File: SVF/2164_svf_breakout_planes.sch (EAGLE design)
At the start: 87 parts, among them IC1 SSM2164P, IC2 TL072, IC3 TL072, IC4 TL072, IC5 TL072, IC6 TL072, U1 THONKICONNNEW, U2 THONKICONNNEW, U3 THONKICONNNEW, U4 THONKICONNNEW, U5 THONKICONNNEW, U6 THONKICONNNEW

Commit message: Add copyright notice
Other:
- note added: "Copyright (c) 2021 Janne Heikkarainen (janne808@radiofreerobotron.net) All rights reserved"
- note added: "Released under CERN Open Hardware Licence Version 2 - Strongly Reciprocal"
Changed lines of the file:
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@@
 <text x="40.64" y="132.08" size="1.778" layer="91">cv1</text>
 <text x="40.64" y="236.22" size="1.778" layer="91">cv2</text>
+<text x="170.18" y="15.24" size="1.778" layer="91">Copyright (c) 2021 Janne Heikkarainen (janne808@radiofreerobotron.net)
+All rights reserved
+</text>
+<text x="170.18" y="10.16" size="1.778" layer="91">Released under CERN Open Hardware Licence Version 2 - Strongly Reciprocal</text>
 </plain>
 <instances>
@@
 </drawing>
 <compatibility>
+<note version="6.3" minversion="6.2.2" severity="warning">
+Since Version 6.2.2 text objects can contain more than one line,
+which will not be processed correctly with this version.
+</note>
 <note version="8.2" severity="warning">
 Since Version 8.2, EAGLE supports online libraries. The ids

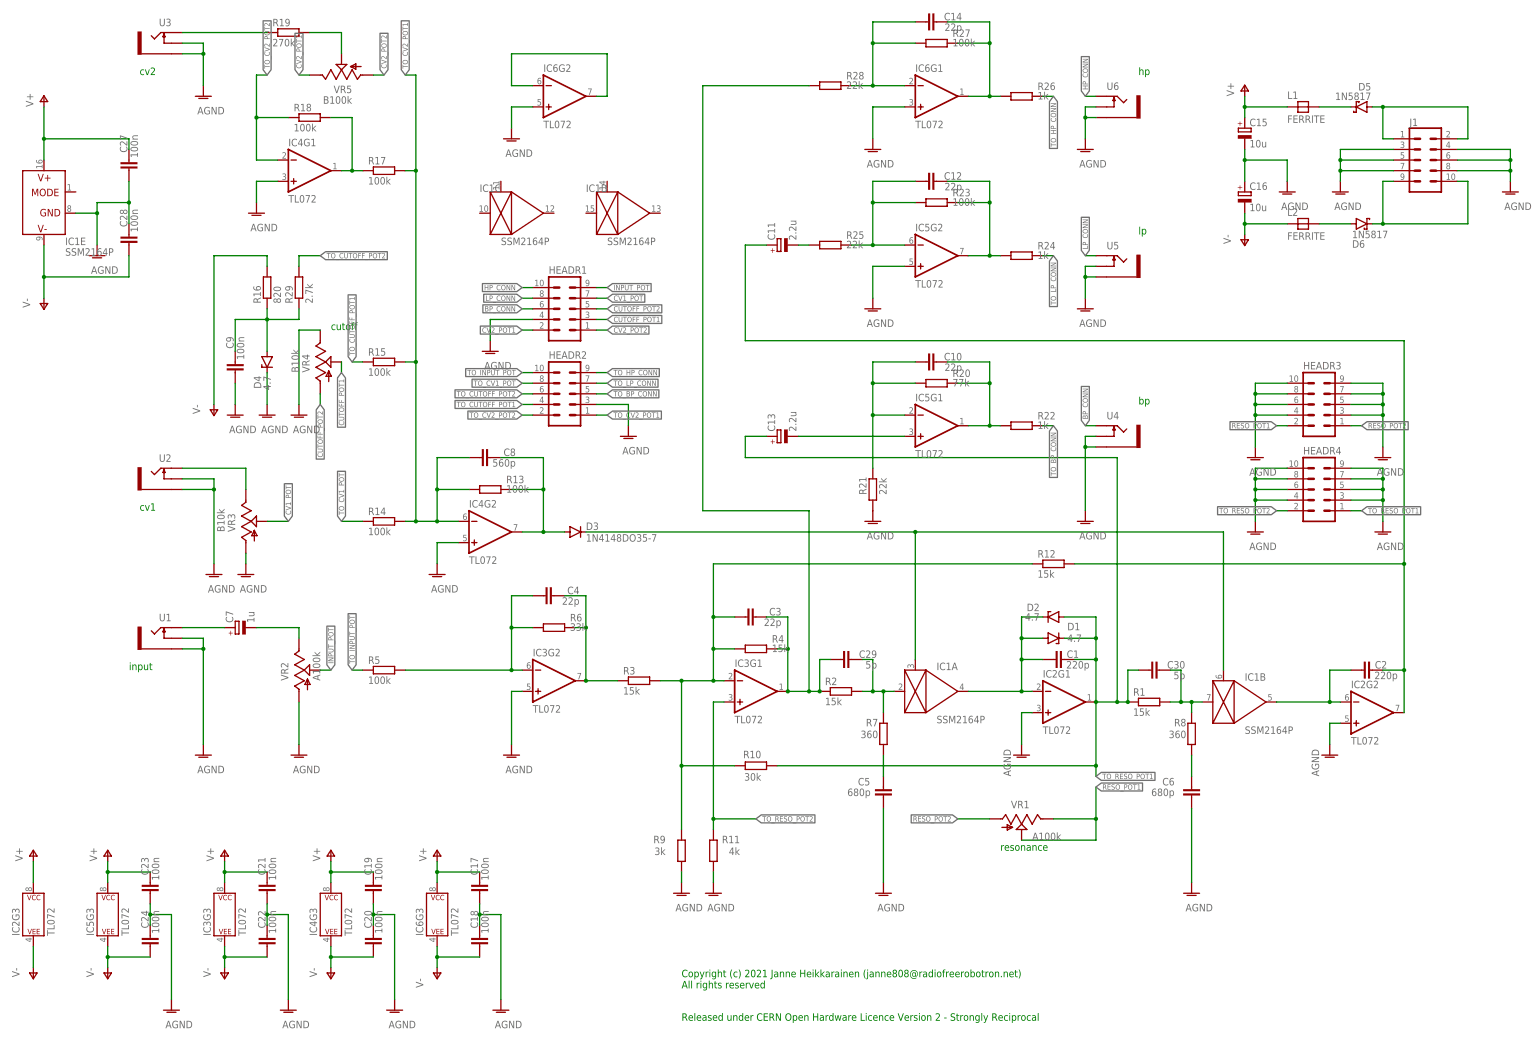
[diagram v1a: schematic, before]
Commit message: Fix backwards footprint graphics for headers and power connector -- note that physical pinouts are unaffected
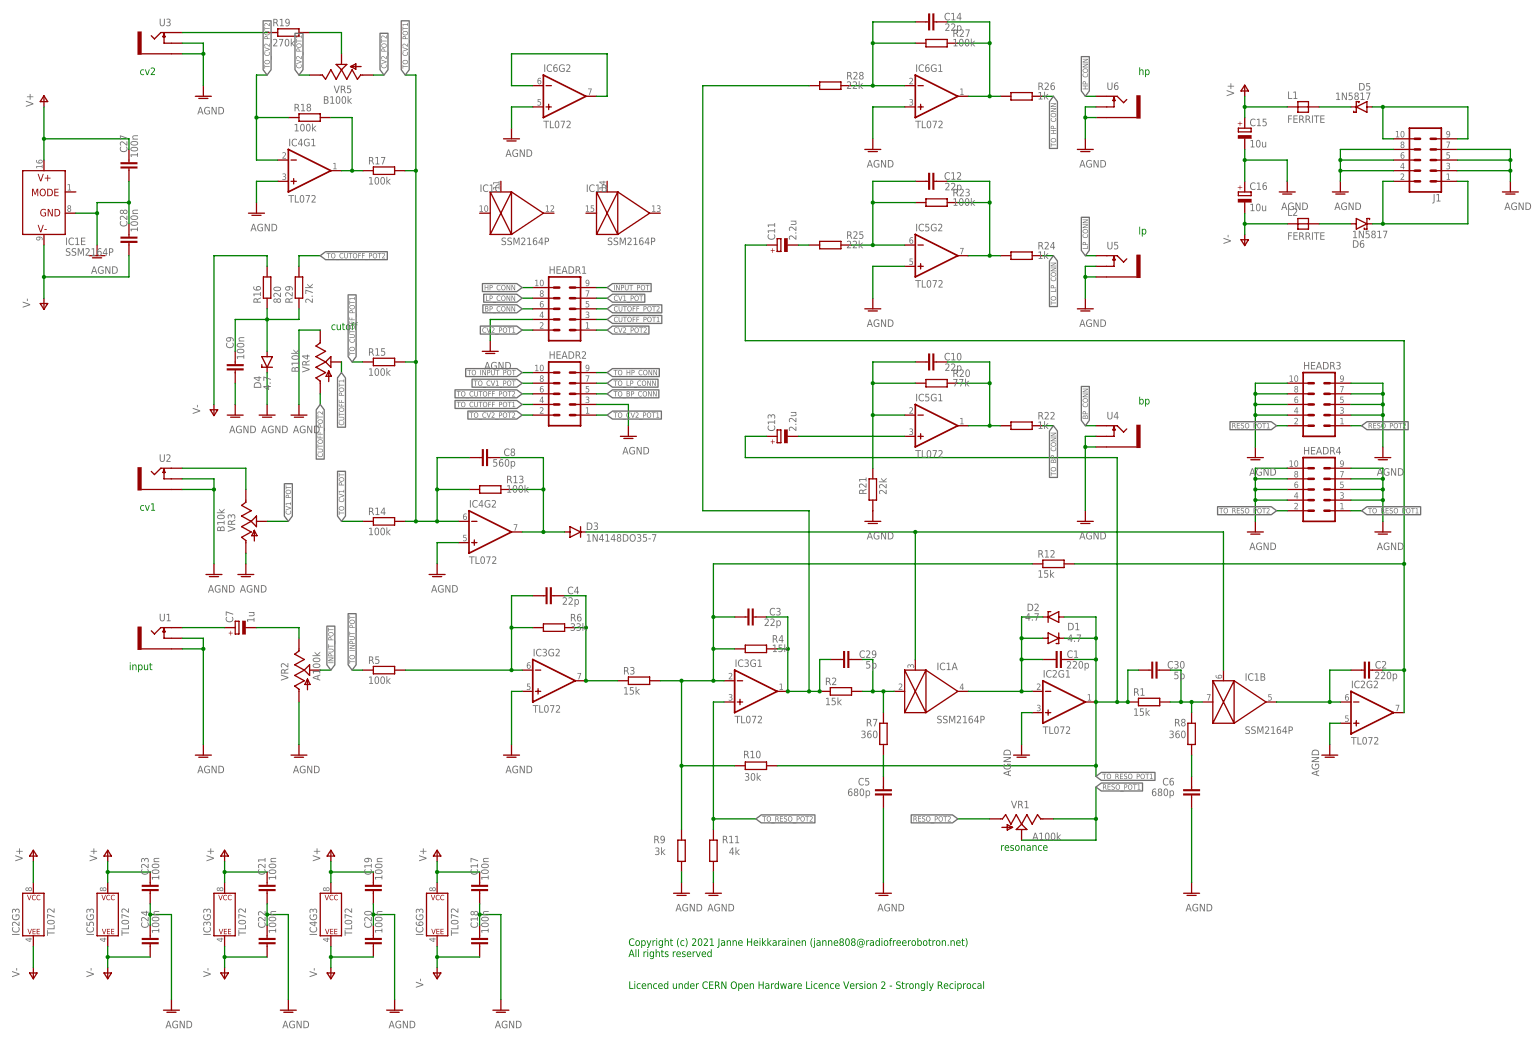
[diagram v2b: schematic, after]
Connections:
- net N$42: now also J1.1, J1.2; no longer J1.10, J1.9
- net N$43: now also J1.10, J1.9; no longer J1.1, J1.2
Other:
- note added: "Licenced under CERN Open Hardware Licence Version 2 - Strongly Reciprocal"
- note removed: "Released under CERN Open Hardware Licence Version 2 - Strongly Reciprocal"
- moved on the sheet: J1
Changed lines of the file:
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@@
 <text x="40.64" y="132.08" size="1.778" layer="91">cv1</text>
 <text x="40.64" y="236.22" size="1.778" layer="91">cv2</text>
-<text x="170.18" y="15.24" size="1.778" layer="91">Copyright (c) 2021 Janne Heikkarainen (janne808@radiofreerobotron.net)
-All rights reserved
-</text>
-<text x="170.18" y="10.16" size="1.778" layer="91">Released under CERN Open Hardware Licence Version 2 - Strongly Reciprocal</text>
+<text x="157.48" y="25.4" size="1.778" layer="91">Copyright (c) 2021 Janne Heikkarainen (janne808@radiofreerobotron.net)
+All rights reserved</text>
+<text x="157.48" y="17.78" size="1.778" layer="91">Licenced under CERN Open Hardware Licence Version 2 - Strongly Reciprocal</text>
 </plain>
 <instances>
@@
 <attribute name="VALUE" x="134.62" y="218.44" size="1.778" layer="96" rot="R180"/>
 </instance>
-<instance part="J1" gate="G$1" x="347.98" y="215.9" smashed="yes">
-<attribute name="VALUE" x="344.17" y="205.994" size="1.778" layer="96" font="vector"/>
-<attribute name="NAME" x="344.17" y="224.028" size="1.778" layer="95" font="vector"/>
+<instance part="J1" gate="G$1" x="347.98" y="215.9" smashed="yes" rot="R180">
+<attribute name="VALUE" x="351.79" y="225.806" size="1.778" layer="96" font="vector" rot="R180"/>
+<attribute name="NAME" x="351.79" y="207.772" size="1.778" layer="95" font="vector" rot="R180"/>
 </instance>
 <instance part="AGND25" gate="VR1" x="368.3" y="208.28" smashed="yes">
@@
 <pinref part="AGND25" gate="VR1" pin="AGND"/>
 <wire x1="368.3" y1="210.82" x2="368.3" y2="213.36" width="0.1524" layer="91"/>
-<pinref part="J1" gate="G$1" pin="4"/>
+<pinref part="J1" gate="G$1" pin="7"/>
 <wire x1="368.3" y1="213.36" x2="368.3" y2="215.9" width="0.1524" layer="91"/>
 <wire x1="368.3" y1="215.9" x2="368.3" y2="218.44" width="0.1524" layer="91"/>
-<wire x1="368.3" y1="218.44" x2="355.6" y2="218.44" width="0.1524" layer="91"/>
-<pinref part="J1" gate="G$1" pin="6"/>
+<wire x1="355.6" y1="218.44" x2="368.3" y2="218.44" width="0.1524" layer="91"/>
+<pinref part="J1" gate="G$1" pin="5"/>
 <wire x1="355.6" y1="215.9" x2="368.3" y2="215.9" width="0.1524" layer="91"/>
 <junction x="368.3" y="215.9"/>
-<pinref part="J1" gate="G$1" pin="8"/>
+<pinref part="J1" gate="G$1" pin="3"/>
 <wire x1="355.6" y1="213.36" x2="368.3" y2="213.36" width="0.1524" layer="91"/>
 <junction x="368.3" y="213.36"/>
@@
 <pinref part="AGND26" gate="VR1" pin="AGND"/>
 <wire x1="327.66" y1="210.82" x2="327.66" y2="213.36" width="0.1524" layer="91"/>
-<pinref part="J1" gate="G$1" pin="3"/>
+<pinref part="J1" gate="G$1" pin="8"/>
 <wire x1="327.66" y1="213.36" x2="327.66" y2="215.9" width="0.1524" layer="91"/>
 <wire x1="327.66" y1="215.9" x2="327.66" y2="218.44" width="0.1524" layer="91"/>
 <wire x1="327.66" y1="218.44" x2="340.36" y2="218.44" width="0.1524" layer="91"/>
-<pinref part="J1" gate="G$1" pin="5"/>
+<pinref part="J1" gate="G$1" pin="6"/>
 <wire x1="340.36" y1="215.9" x2="327.66" y2="215.9" width="0.1524" layer="91"/>
 <junction x="327.66" y="215.9"/>
-<pinref part="J1" gate="G$1" pin="7"/>
+<pinref part="J1" gate="G$1" pin="4"/>
 <wire x1="340.36" y1="213.36" x2="327.66" y2="213.36" width="0.1524" layer="91"/>
 <junction x="327.66" y="213.36"/>
@@
 <net name="N$42" class="0">
 <segment>
-<pinref part="J1" gate="G$1" pin="9"/>
-<wire x1="340.36" y1="210.82" x2="337.82" y2="210.82" width="0.1524" layer="91"/>
 <pinref part="D6" gate="G$1" pin="C"/>
 <wire x1="335.28" y1="200.66" x2="337.82" y2="200.66" width="0.1524" layer="91"/>
@@
 <wire x1="337.82" y1="200.66" x2="358.14" y2="200.66" width="0.1524" layer="91"/>
 <junction x="337.82" y="200.66"/>
+<wire x1="358.14" y1="200.66" x2="358.14" y2="210.82" width="0.1524" layer="91"/>
+<pinref part="J1" gate="G$1" pin="2"/>
+<wire x1="340.36" y1="210.82" x2="337.82" y2="210.82" width="0.1524" layer="91"/>
+<pinref part="J1" gate="G$1" pin="1"/>
+<wire x1="355.6" y1="210.82" x2="358.14" y2="210.82" width="0.1524" layer="91"/>
+</segment>
+</net>
+<net name="N$43" class="0">
+<segment>
+<pinref part="D5" gate="G$1" pin="A"/>
+<wire x1="335.28" y1="228.6" x2="337.82" y2="228.6" width="0.1524" layer="91"/>
 <pinref part="J1" gate="G$1" pin="10"/>
-<wire x1="358.14" y1="210.82" x2="355.6" y2="210.82" width="0.1524" layer="91"/>
-<wire x1="358.14" y1="200.66" x2="358.14" y2="210.82" width="0.1524" layer="91"/>
-</segment>
-</net>
-<net name="N$43" class="0">
-<segment>
-<pinref part="J1" gate="G$1" pin="1"/>
+<wire x1="337.82" y1="228.6" x2="358.14" y2="228.6" width="0.1524" layer="91"/>
 <wire x1="340.36" y1="220.98" x2="337.82" y2="220.98" width="0.1524" layer="91"/>
 <wire x1="337.82" y1="220.98" x2="337.82" y2="228.6" width="0.1524" layer="91"/>
-<pinref part="D5" gate="G$1" pin="A"/>
-<wire x1="335.28" y1="228.6" x2="337.82" y2="228.6" width="0.1524" layer="91"/>
-<wire x1="337.82" y1="228.6" x2="358.14" y2="228.6" width="0.1524" layer="91"/>
 <junction x="337.82" y="228.6"/>
-<wire x1="358.14" y1="228.6" x2="358.14" y2="220.98" width="0.1524" layer="91"/>
-<pinref part="J1" gate="G$1" pin="2"/>
-<wire x1="358.14" y1="220.98" x2="355.6" y2="220.98" width="0.1524" layer="91"/>
-</segment>
-</net>
+<pinref part="J1" gate="G$1" pin="9"/>
+<wire x1="355.6" y1="220.98" x2="358.14" y2="220.98" width="0.1524" layer="91"/>
+<wire x1="358.14" y1="220.98" x2="358.14" y2="228.6" width="0.1524" layer="91"/>
+</segment>
+</net>

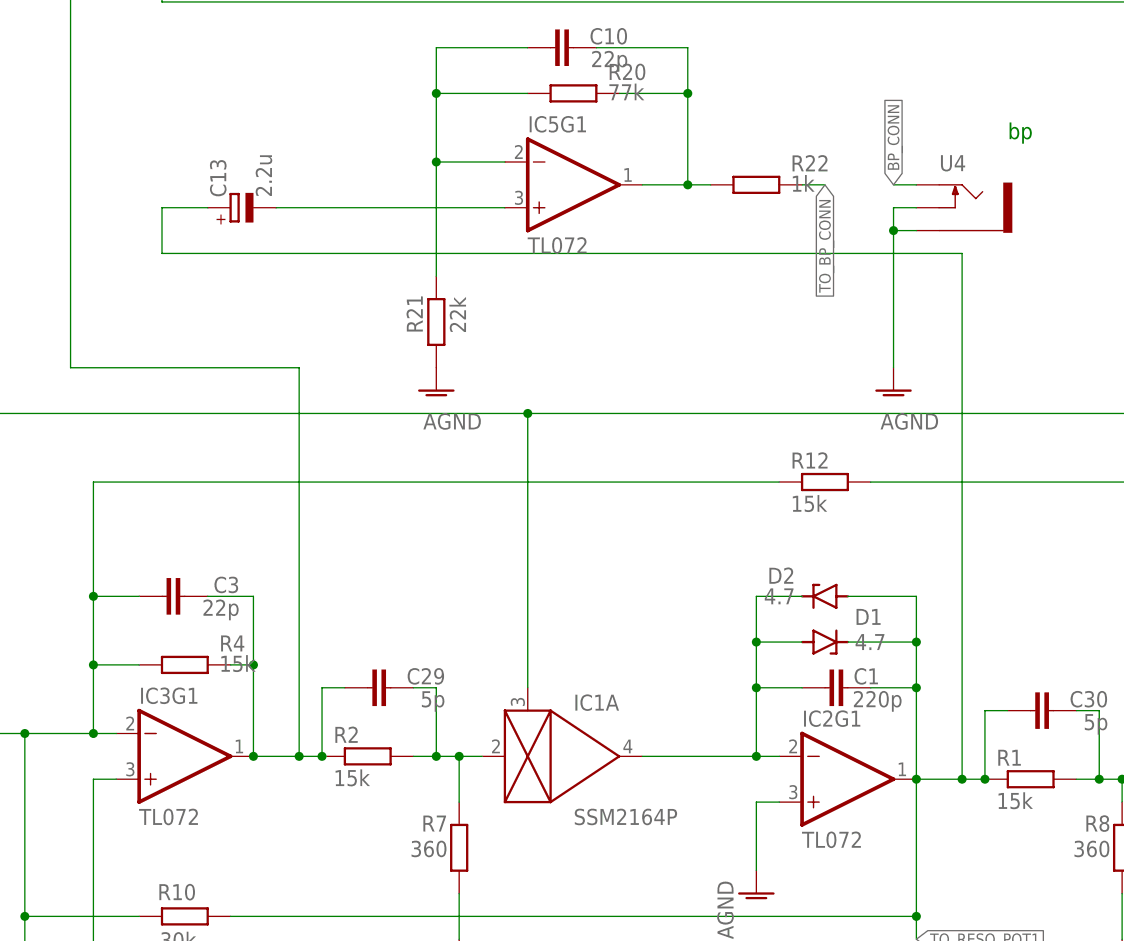
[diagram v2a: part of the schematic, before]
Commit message: Fix bandpass output AC biasing issue
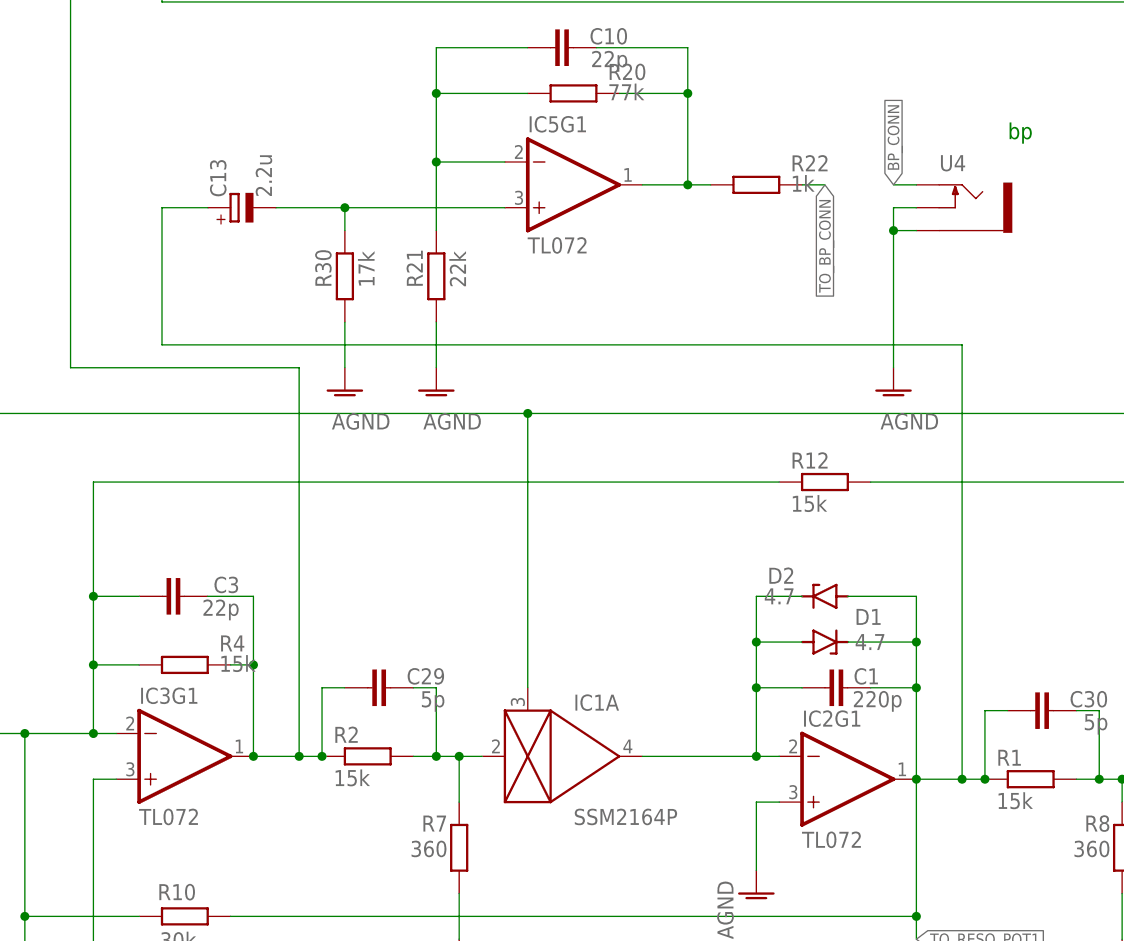
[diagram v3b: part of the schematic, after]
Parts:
- added R30: 17k, rcl:R-EU_0207/2V
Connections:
- removed net N$30: C13.-, IC5G1.+IN
- new net N$3: C13.-, IC5G1.+IN, R30.2
- net AGND: now also R30.1
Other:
- moved on the sheet: R21
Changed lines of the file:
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@@
 <part name="C28" library="rcl" library_urn="urn:adsk.eagle:library:334" deviceset="C-EU" device="050-025X075" package3d_urn="urn:adsk.eagle:package:23637/1" value="100n"/>
 <part name="R29" library="rcl" library_urn="urn:adsk.eagle:library:334" deviceset="R-EU_" device="0207/2V" package3d_urn="urn:adsk.eagle:package:23490/1" value="2.7k"/>
+<part name="R30" library="rcl" library_urn="urn:adsk.eagle:library:334" deviceset="R-EU_" device="0207/2V" package3d_urn="urn:adsk.eagle:package:23490/1" value="17k"/>
+<part name="AGND39" library="supply1" library_urn="urn:adsk.eagle:library:371" deviceset="AGND" device=""/>
 </parts>
 <sheets>
@@
 <attribute name="VALUE" x="234.95" y="161.798" size="1.778" layer="96"/>
 </instance>
-<instance part="R21" gate="G$1" x="215.9" y="137.16" smashed="yes" rot="R90">
-<attribute name="NAME" x="214.4014" y="135.89" size="1.778" layer="95" rot="R90"/>
-<attribute name="VALUE" x="219.202" y="135.89" size="1.778" layer="96" rot="R90"/>
+<instance part="R21" gate="G$1" x="215.9" y="142.24" smashed="yes" rot="R90">
+<attribute name="NAME" x="214.4014" y="140.97" size="1.778" layer="95" rot="R90"/>
+<attribute name="VALUE" x="219.202" y="140.97" size="1.778" layer="96" rot="R90"/>
 </instance>
 <instance part="R22" gate="G$1" x="251.46" y="152.4" smashed="yes">
@@
 <attribute name="NAME" x="77.2414" y="181.61" size="1.778" layer="95" rot="R90"/>
 <attribute name="VALUE" x="82.042" y="181.61" size="1.778" layer="96" rot="R90"/>
+</instance>
+<instance part="R30" gate="G$1" x="205.74" y="142.24" smashed="yes" rot="R90">
+<attribute name="NAME" x="204.2414" y="140.97" size="1.778" layer="95" rot="R90"/>
+<attribute name="VALUE" x="209.042" y="140.97" size="1.778" layer="96" rot="R90"/>
+</instance>
+<instance part="AGND39" gate="VR1" x="205.74" y="129.54" smashed="yes">
+<attribute name="VALUE" x="210.82" y="127" size="1.778" layer="96" rot="R180"/>
 </instance>
 </instances>
@@
 <pinref part="AGND18" gate="VR1" pin="AGND"/>
 <pinref part="R21" gate="G$1" pin="1"/>
+<wire x1="215.9" y1="137.16" x2="215.9" y2="132.08" width="0.1524" layer="91"/>
 </segment>
 <segment>
@@
 <wire x1="48.26" y1="35.56" x2="43.18" y2="35.56" width="0.1524" layer="91"/>
 <junction x="43.18" y="35.56"/>
+</segment>
+<segment>
+<pinref part="AGND39" gate="VR1" pin="AGND"/>
+<pinref part="R30" gate="G$1" pin="1"/>
+<wire x1="205.74" y1="132.08" x2="205.74" y2="137.16" width="0.1524" layer="91"/>
 </segment>
 </net>
@@
 <wire x1="269.24" y1="71.12" x2="269.24" y2="86.36" width="0.1524" layer="91"/>
 <wire x1="193.04" y1="71.12" x2="269.24" y2="71.12" width="0.1524" layer="91"/>
-<wire x1="274.32" y1="86.36" x2="274.32" y2="144.78" width="0.1524" layer="91"/>
-<wire x1="274.32" y1="144.78" x2="185.42" y2="144.78" width="0.1524" layer="91"/>
+<wire x1="274.32" y1="86.36" x2="274.32" y2="134.62" width="0.1524" layer="91"/>
+<wire x1="274.32" y1="134.62" x2="185.42" y2="134.62" width="0.1524" layer="91"/>
 <junction x="274.32" y="86.36"/>
-<wire x1="185.42" y1="144.78" x2="185.42" y2="149.86" width="0.1524" layer="91"/>
+<wire x1="185.42" y1="134.62" x2="185.42" y2="149.86" width="0.1524" layer="91"/>
 <wire x1="185.42" y1="149.86" x2="190.5" y2="149.86" width="0.1524" layer="91"/>
 <pinref part="C13" gate="G$1" pin="+"/>
@@
 <segment>
 <pinref part="R21" gate="G$1" pin="2"/>
-<wire x1="215.9" y1="142.24" x2="215.9" y2="154.94" width="0.1524" layer="91"/>
+<wire x1="215.9" y1="147.32" x2="215.9" y2="154.94" width="0.1524" layer="91"/>
 <pinref part="IC5" gate="G1" pin="-IN"/>
 <wire x1="215.9" y1="154.94" x2="223.52" y2="154.94" width="0.1524" layer="91"/>
@@
 <wire x1="243.84" y1="167.64" x2="243.84" y2="162.56" width="0.1524" layer="91"/>
 <junction x="243.84" y="162.56"/>
-</segment>
-</net>
-<net name="N$30" class="0">
-<segment>
-<pinref part="IC5" gate="G1" pin="+IN"/>
-<wire x1="198.12" y1="149.86" x2="223.52" y2="149.86" width="0.1524" layer="91"/>
-<pinref part="C13" gate="G$1" pin="-"/>
 </segment>
 </net>
@@
 </segment>
 </net>
+<net name="N$3" class="0">
+<segment>
+<pinref part="C13" gate="G$1" pin="-"/>
+<wire x1="198.12" y1="149.86" x2="205.74" y2="149.86" width="0.1524" layer="91"/>
+<pinref part="R30" gate="G$1" pin="2"/>
+<wire x1="205.74" y1="149.86" x2="205.74" y2="147.32" width="0.1524" layer="91"/>
+<pinref part="IC5" gate="G1" pin="+IN"/>
+<wire x1="205.74" y1="149.86" x2="223.52" y2="149.86" width="0.1524" layer="91"/>
+<junction x="205.74" y="149.86"/>
+</segment>
+</net>
